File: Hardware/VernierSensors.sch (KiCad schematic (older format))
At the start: 6 parts

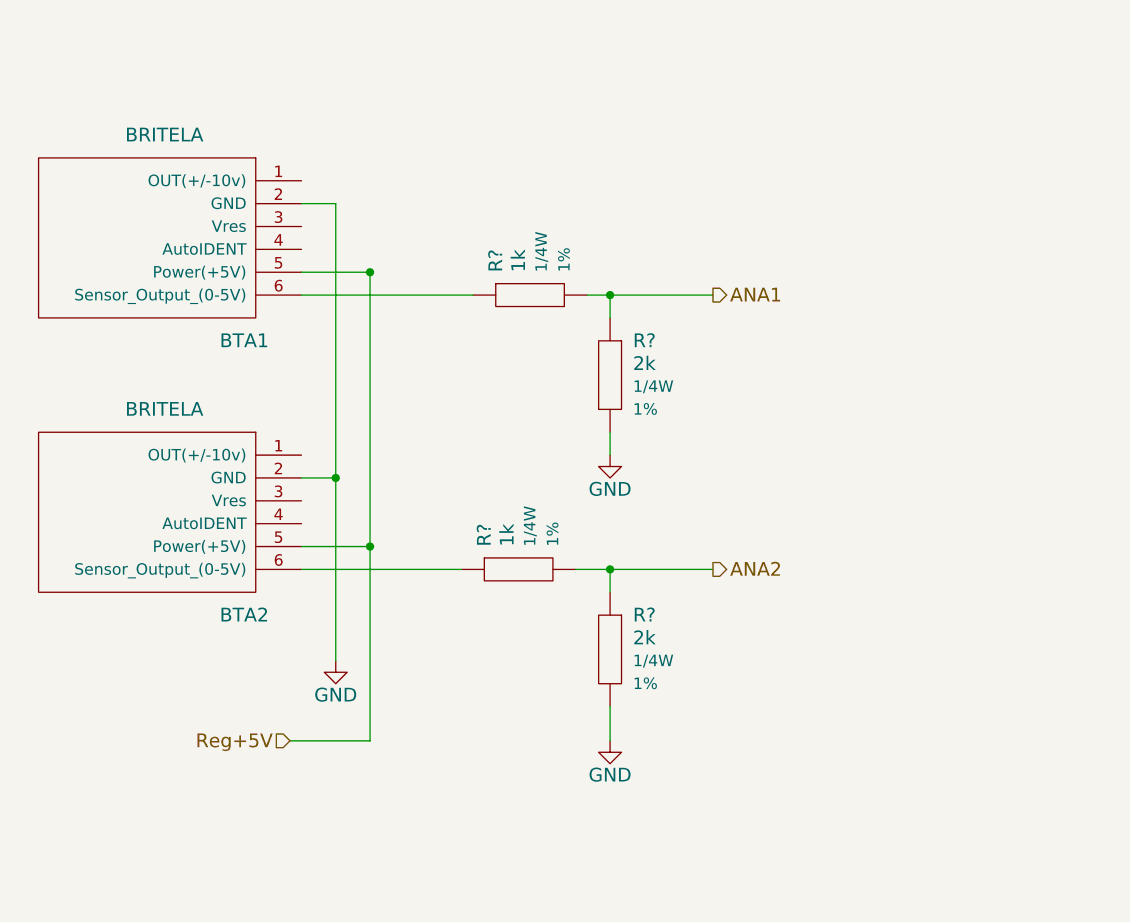
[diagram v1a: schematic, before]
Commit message: Add instrumentation amplifier for load cell, added amplifiers for ph and moisture sensors
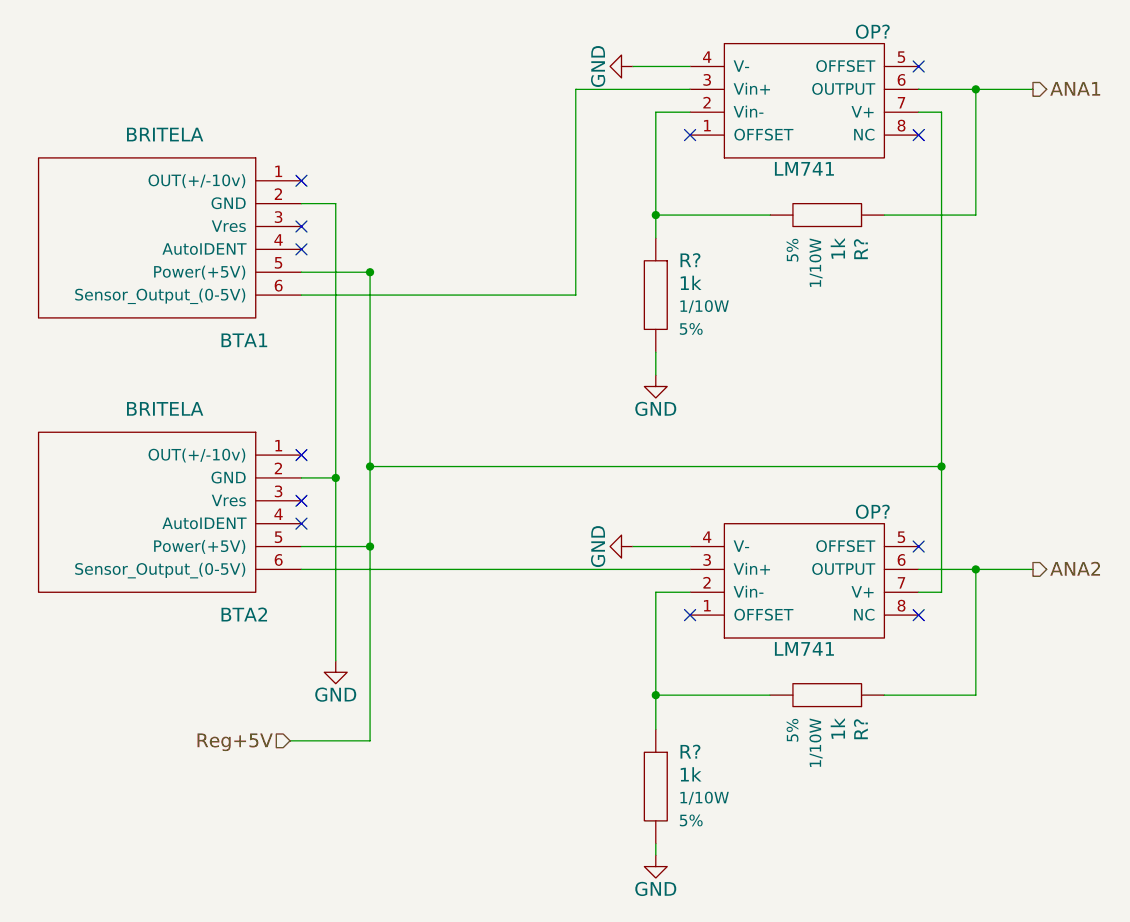
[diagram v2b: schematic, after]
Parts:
- removed R? (x2): 1k, 1206, symbol Resistor
- removed R? (x2): 2k, 1206, symbol Resistor
- added OP? (x2): LM741, symbol LM741
- added R? (x4): 1k, symbol Resistor
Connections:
- net ANA1: now also OP?.6 (OUTPUT), R?.1
- net ANA2: now also OP?.6 (OUTPUT), R?.1
- net GND: now also OP?.4 (V-), OP?.4 (V-), R?.2, R?.2
- net Reg+5V: now also OP?.7 (V+), OP?.7 (V+)
- net at BTA1.6 (Sensor_Output_(0-5V)): now also OP?.3 (Vin+)
- net at BTA2.6 (Sensor_Output_(0-5V)): now also OP?.3 (Vin+)
- new net: OP?.2 (Vin-), R?.1, R?.2 (x2)
- no-connect marks 0 -> 12

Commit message: Add GPS Pads, potentiometer to INA125, 3v3 regulator always enabled, footprints created for GPS Pads and BTA, parts assigned
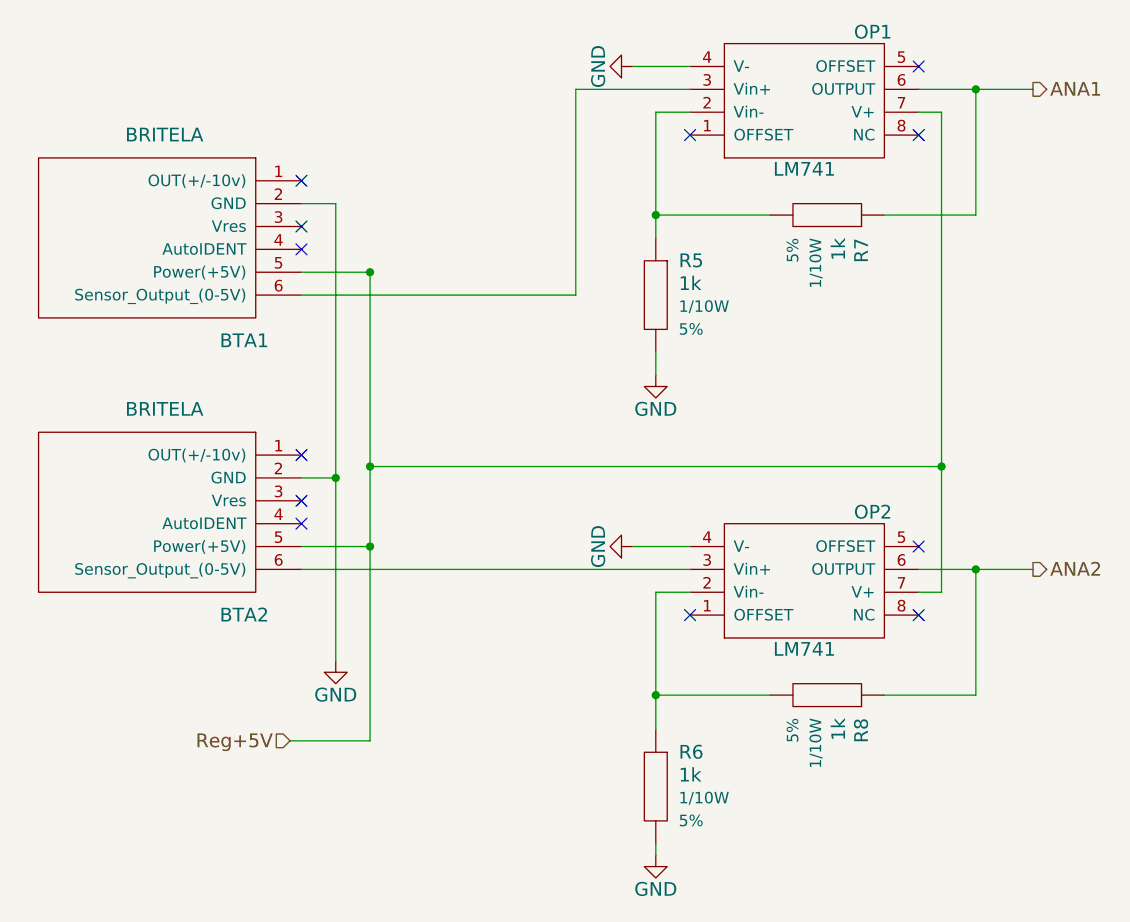
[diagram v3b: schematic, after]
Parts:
- removed OP?: LM741, symbol LM741
- added OP2: LM741, Housings_SOIC:SOIC-8_3.9x4.9mm_Pitch1.27mm, symbol LM741
- BTA1, BTA2: footprint (none) -> MAVRIc:BTA
- OP1: renamed from OP?; footprint (none) -> Housings_SOIC:SOIC-8_3.9x4.9mm_Pitch1.27mm; Manufacturer (none) -> DigiKey; Manufacturer SKU (none) -> 296-15051-1-ND
- R5, R6, R7, R8: renamed from R?; footprint (none) -> Resistors_SMD:R_1206_HandSoldering
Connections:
- net ANA2: now also OP2.6 (OUTPUT)
- net GND: now also OP2.4 (V-)
- net Reg+5V: now also OP2.7 (V+)
- net at BTA2.6 (Sensor_Output_(0-5V)): now also OP2.3 (Vin+)
- net at R6.1, R8.2: now also OP2.2 (Vin-)
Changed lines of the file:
@@
 F 0 "BTA1" H 2500 1700 60  0000 C CNN
 F 1 "BRITELA" H 2150 2600 60  0000 C CNN
-F 2 "" H 1800 2300 60  0000 C CNN
+F 2 "MAVRIc:BTA" H 1800 2300 60  0001 C CNN
 F 3 "" H 1800 2300 60  0000 C CNN
 	1    2150 2200
@@
 F 0 "BTA2" H 2500 2900 60  0000 C CNN
 F 1 "BRITELA" H 2150 3800 60  0000 C CNN
-F 2 "" H 1800 3500 60  0000 C CNN
+F 2 "MAVRIc:BTA" H 1800 3500 60  0001 C CNN
 F 3 "" H 1800 3500 60  0000 C CNN
 	1    2150 3400
@@
 Reg+5V
 Wire Wire Line
-	3050 2400 3050 3250
-Wire Wire Line
-	3050 3250 3050 3600
-Wire Wire Line
-	3050 3600 3050 4450
+	3050 2400 3050 4450
 Wire Wire Line
 	3050 3600 2750 3600
@@
 	2750 2100 2900 2100
 Wire Wire Line
-	2900 2100 2900 3300
-Wire Wire Line
-	2900 3300 2900 4100
+	2900 2100 2900 4100
 Wire Wire Line
 	2900 3300 2750 3300
 Connection ~ 2900 3300
 $Comp
-L GND #PWR1
+L GND #PWR018
 U 1 1 551E15A1
 P 2900 4100
-F 0 "#PWR1" H 2900 3850 60  0001 C CNN
+F 0 "#PWR018" H 2900 3850 60  0001 C CNN
 F 1 "GND" H 2900 3950 60  0000 C CNN
 F 2 "" H 2900 4100 60  0000 C CNN
@@
 	2750 3700 4450 3700
 $Comp
-L LM741 OP?
+L LM741 OP1
 U 1 1 5536B2A8
 P 4950 1650
-F 0 "OP?" H 5250 1350 60  0000 C CNN
+F 0 "OP1" H 5250 1350 60  0000 C CNN
 F 1 "LM741" H 4950 1950 60  0000 C CNN
-F 2 "" H 4850 1600 60  0000 C CNN
+F 2 "Housings_SOIC:SOIC-8_3.9x4.9mm_Pitch1.27mm" H 4850 1600 60  0001 C CNN
 F 3 "" H 4850 1600 60  0000 C CNN
+F 4 "DigiKey" H 4950 1650 60  0001 C CNN "Manufacturer"
+F 5 "296-15051-1-ND" H 4950 1650 60  0001 C CNN "Manufacturer SKU"
 	1    4950 1650
 	1    0    0    1
@@
 	4450 1700 4300 1700
 Wire Wire Line
-	4300 1700 4300 2150
-Wire Wire Line
-	4300 2150 4300 2250
-$Comp
-L Resistor R?
+	4300 1700 4300 2250
+$Comp
+L Resistor R5
 U 1 1 5536BEE4
 P 4300 2500
-F 0 "R?" V 4150 2600 60  0000 L CNN
+F 0 "R5" V 4150 2600 60  0000 L CNN
 F 1 "1k" V 4250 2600 60  0000 L CNN
-F 2 "" H 4200 2500 60  0001 C CNN
+F 2 "Resistors_SMD:R_1206_HandSoldering" H 4200 2500 60  0001 C CNN
 F 3 "" H 4300 2600 60  0001 C CNN
 F 4 "Value" H 4300 2500 60  0001 C CNN "Manufacturer"
@@
 $EndComp
 $Comp
-L Resistor R?
+L Resistor R7
 U 1 1 5536BF5F
 P 5050 2150
-F 0 "R?" V 4900 2250 60  0000 L CNN
+F 0 "R7" V 4900 2250 60  0000 L CNN
 F 1 "1k" V 5000 2250 60  0000 L CNN
-F 2 "" H 4950 2150 60  0001 C CNN
+F 2 "Resistors_SMD:R_1206_HandSoldering" H 4950 2150 60  0001 C CNN
 F 3 "" H 5050 2250 60  0001 C CNN
 F 4 "Value" H 5050 2150 60  0001 C CNN "Manufacturer"
@@
 	5700 2150 5700 1600
 Wire Wire Line
-	5450 1600 5700 1600
-Wire Wire Line
-	5700 1600 5950 1600
-$Comp
-L GND #PWR?
+	5450 1600 5950 1600
+$Comp
+L GND #PWR019
 U 1 1 5536C048
 P 4300 2850
-F 0 "#PWR?" H 4300 2600 60  0001 C CNN
+F 0 "#PWR019" H 4300 2600 60  0001 C CNN
 F 1 "GND" H 4300 2700 60  0000 C CNN
 F 2 "" H 4300 2850 60  0000 C CNN
@@
 	4300 2850 4300 2750
 Connection ~ 5700 1600
-$Comp
-L LM741 OP?
-U 1 1 5536C358
-P 4950 3750
-F 0 "OP?" H 5250 3450 60  0000 C CNN
-F 1 "LM741" H 4950 4050 60  0000 C CNN
-F 2 "" H 4850 3700 60  0000 C CNN
-F 3 "" H 4850 3700 60  0000 C CNN
-	1    4950 3750
-	1    0    0    1
-$EndComp
 Wire Wire Line
 	4450 3800 4300 3800
 Wire Wire Line
-	4300 3800 4300 4250
-Wire Wire Line
-	4300 4250 4300 4400
-$Comp
-L Resistor R?
+	4300 3800 4300 4400
+$Comp
+L Resistor R6
 U 1 1 5536C369
 P 4300 4650
-F 0 "R?" V 4150 4750 60  0000 L CNN
+F 0 "R6" V 4150 4750 60  0000 L CNN
 F 1 "1k" V 4250 4750 60  0000 L CNN
-F 2 "" H 4200 4650 60  0001 C CNN
+F 2 "Resistors_SMD:R_1206_HandSoldering" H 4200 4650 60  0001 C CNN
 F 3 "" H 4300 4750 60  0001 C CNN
 F 4 "Value" H 4300 4650 60  0001 C CNN "Manufacturer"
@@
 $EndComp
 $Comp
-L Resistor R?
+L Resistor R8
 U 1 1 5536C375
 P 5050 4250
-F 0 "R?" V 4900 4350 60  0000 L CNN
+F 0 "R8" V 4900 4350 60  0000 L CNN
 F 1 "1k" V 5000 4350 60  0000 L CNN
-F 2 "" H 4950 4250 60  0001 C CNN
+F 2 "Resistors_SMD:R_1206_HandSoldering" H 4950 4250 60  0001 C CNN
 F 3 "" H 5050 4350 60  0001 C CNN
 F 4 "Value" H 5050 4250 60  0001 C CNN "Manufacturer"
@@
 	5700 4250 5700 3700
 Wire Wire Line
-	5450 3700 5700 3700
-Wire Wire Line
-	5700 3700 5950 3700
-$Comp
-L GND #PWR?
+	5450 3700 5950 3700
+$Comp
+L GND #PWR020
 U 1 1 5536C381
 P 4300 4950
-F 0 "#PWR?" H 4300 4700 60  0001 C CNN
+F 0 "#PWR020" H 4300 4700 60  0001 C CNN
 F 1 "GND" H 4300 4800 60  0000 C CNN
 F 2 "" H 4300 4950 60  0000 C CNN
@@
 Connection ~ 5700 3700
 $Comp
-L GND #PWR?
+L GND #PWR021
 U 1 1 5536CDD6
 P 4200 3600
-F 0 "#PWR?" H 4200 3350 60  0001 C CNN
+F 0 "#PWR021" H 4200 3350 60  0001 C CNN
 F 1 "GND" H 4200 3450 60  0000 C CNN
 F 2 "" H 4200 3600 60  0000 C CNN
@@
 	4450 1500 4200 1500
 $Comp
-L GND #PWR?
+L GND #PWR022
 U 1 1 5536CE79
 P 4200 1500
-F 0 "#PWR?" H 4200 1250 60  0001 C CNN
+F 0 "#PWR022" H 4200 1250 60  0001 C CNN
 F 1 "GND" H 4200 1350 60  0000 C CNN
 F 2 "" H 4200 1500 60  0000 C CNN
@@
 $EndComp
 Wire Wire Line
-	5450 3800 5550 3800
-Wire Wire Line
-	5550 3800 5550 3250
-Wire Wire Line
-	5550 3250 5550 1700
+	5550 3800 5450 3800
+Wire Wire Line
+	5550 1700 5550 3800
 Wire Wire Line
 	5550 1700 5450 1700
@@
 NoConn ~ 2750 3400
 NoConn ~ 2750 3500
+$Comp
+L LM741 OP2
+U 1 1 553F213B
+P 4950 3750
+F 0 "OP2" H 5250 3450 60  0000 C CNN
+F 1 "LM741" H 4950 4050 60  0000 C CNN
+F 2 "Housings_SOIC:SOIC-8_3.9x4.9mm_Pitch1.27mm" H 4850 3700 60  0001 C CNN
+F 3 "" H 4850 3700 60  0000 C CNN
+F 4 "DigiKey" H 4950 3750 60  0001 C CNN "Manufacturer"
+F 5 "296-15051-1-ND" H 4950 3750 60  0001 C CNN "Manufacturer SKU"
+	1    4950 3750
+	1    0    0    1
+$EndComp
 $EndSCHEMATC
